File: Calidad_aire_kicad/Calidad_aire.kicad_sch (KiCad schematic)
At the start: 10 parts, among them J1 Micro_SD_Card, U1 DOIT-ESP32-DEVKIT-V1

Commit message: start to PCB design
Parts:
- A1, A4: footprint (none) -> footprint_project:header_4pos_1row
- U1: footprint (none) -> footprint_project:ESP32_DEVKIT1
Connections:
- net 3.3V: now also A4.3 (VCC), U1.16 (3V3); no longer A4. (VCC), U1.19 (3V3)
- net 5V: now also A1.1 (5V), A2.3 (5V), A3.3 (5V), U1.15 (VIN); no longer A1. (GND), A2. (TX), A3. (TX), U1.18 (VIN)
- net GND: now also A1.2 (GND), A2.4 (GND), A3.4 (GND), A4.4 (GND), A5.3 (NC), U1.14 (GND); no longer A1. (GND), A2. (TX), A3. (TX), A4. (VCC), A5.4 (GND), U1.17 (GND)
- net RX0_3V: now also A2.2 (TX); no longer A2. (TX)
- net RX0_5V: now also U1.27 (GPIO3__UART0-RX); no longer U1.33 (GPIO3__UART0-RX)
- net RX2_3V: now also A3.2 (TX); no longer A3. (TX)
- net RX2_5V: now also U1.21 (GPIO16_UART2-RX); no longer U1.27 (GPIO16_UART2-RX)
- net SCK: now also A4.2 (SCK), U1.29 (GPIO22_I2C-SCL); no longer A4. (VCC), U1.35 (GPIO22_I2C-SCL)
- net SDA: now also A4.1 (SDA), U1.26 (GPIO21_I2C-SDA); no longer A4. (VCC), U1.32 (GPIO21_I2C-SDA)
- net SD_CLK: now also U1.24 (GPIO18_VSPI-CLK); no longer U1.30 (GPIO18_VSPI-CLK)
- net SD_MISO: now also U1.25 (GPIO19_VSPI-MISO); no longer U1.31 (GPIO19_VSPI-MISO)
- net SD_MOSI: now also U1.30 (GPIO23_VSPI-MOSI); no longer U1.36 (GPIO23_VSPI-MOSI)
- net SD_SS: now also U1.23 (GPIO5_VSPI-CS0); no longer U1.29 (GPIO5_VSPI-CS0)
- net TX0_3V: now also A2.1 (RX); no longer A2. (TX)
- net TX0_5V: now also U1.28 (GPIO1_UART0-TX); no longer U1.34 (GPIO1_UART0-TX)
- net TX2_3V: now also A3.1 (RX); no longer A3. (TX)
- net TX2_5V: now also U1.22 (GPIO17_UART2-TX); no longer U1.28 (GPIO17_UART2-TX)
- net at R1.1: now also A1.3 (DO); no longer A1. (GND)
- no-connect marks 6 -> 24
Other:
- moved on the sheet: J1

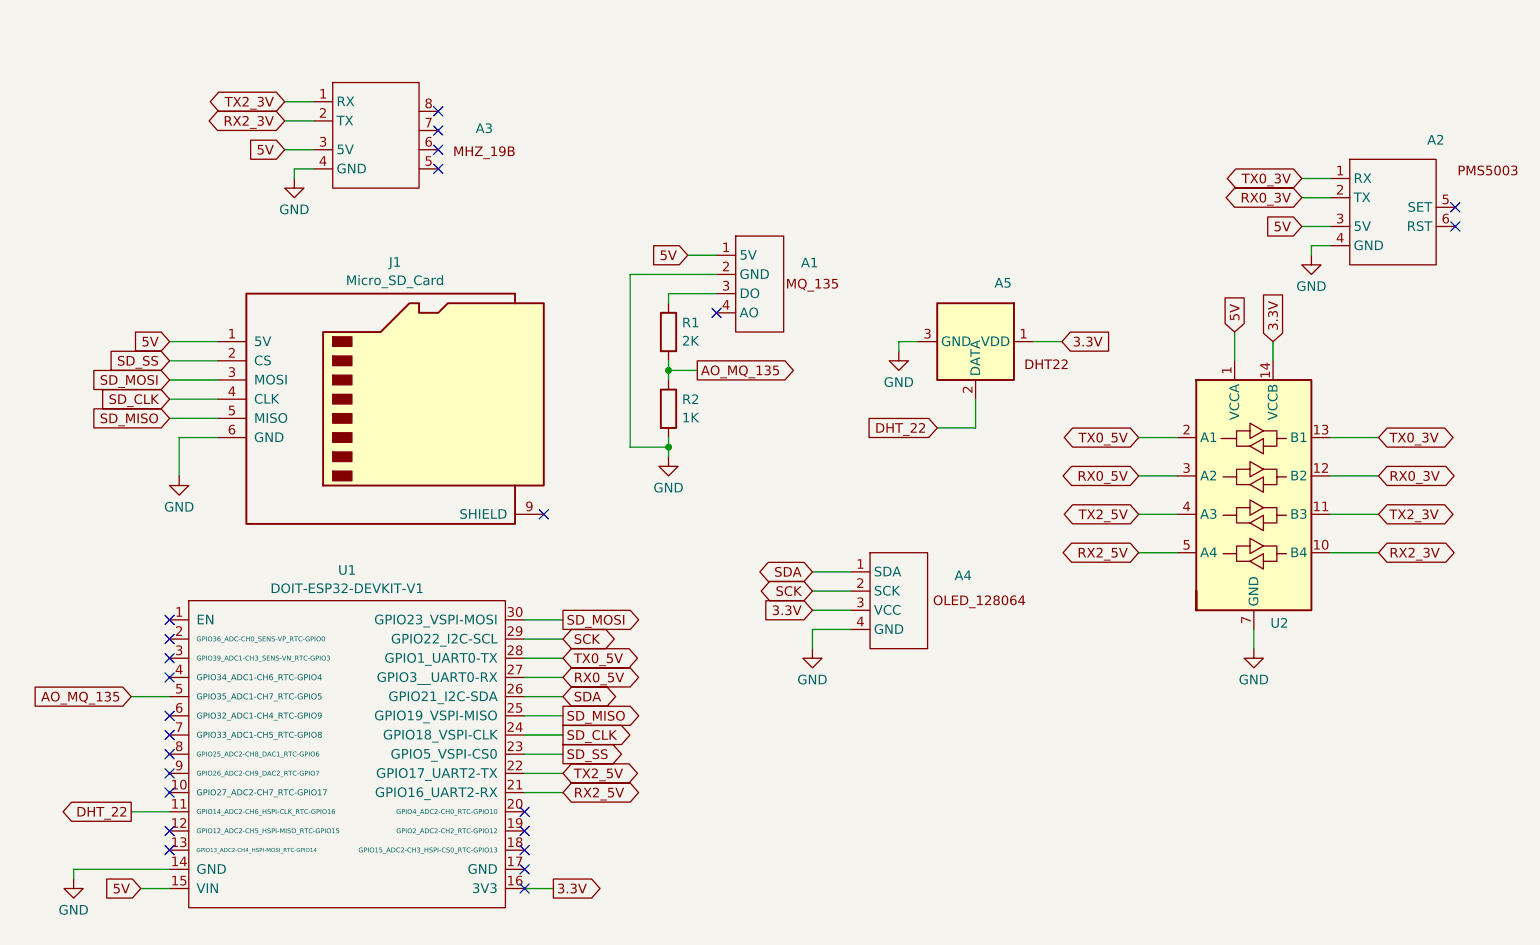
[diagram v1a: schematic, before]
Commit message: design of the footprints for the components
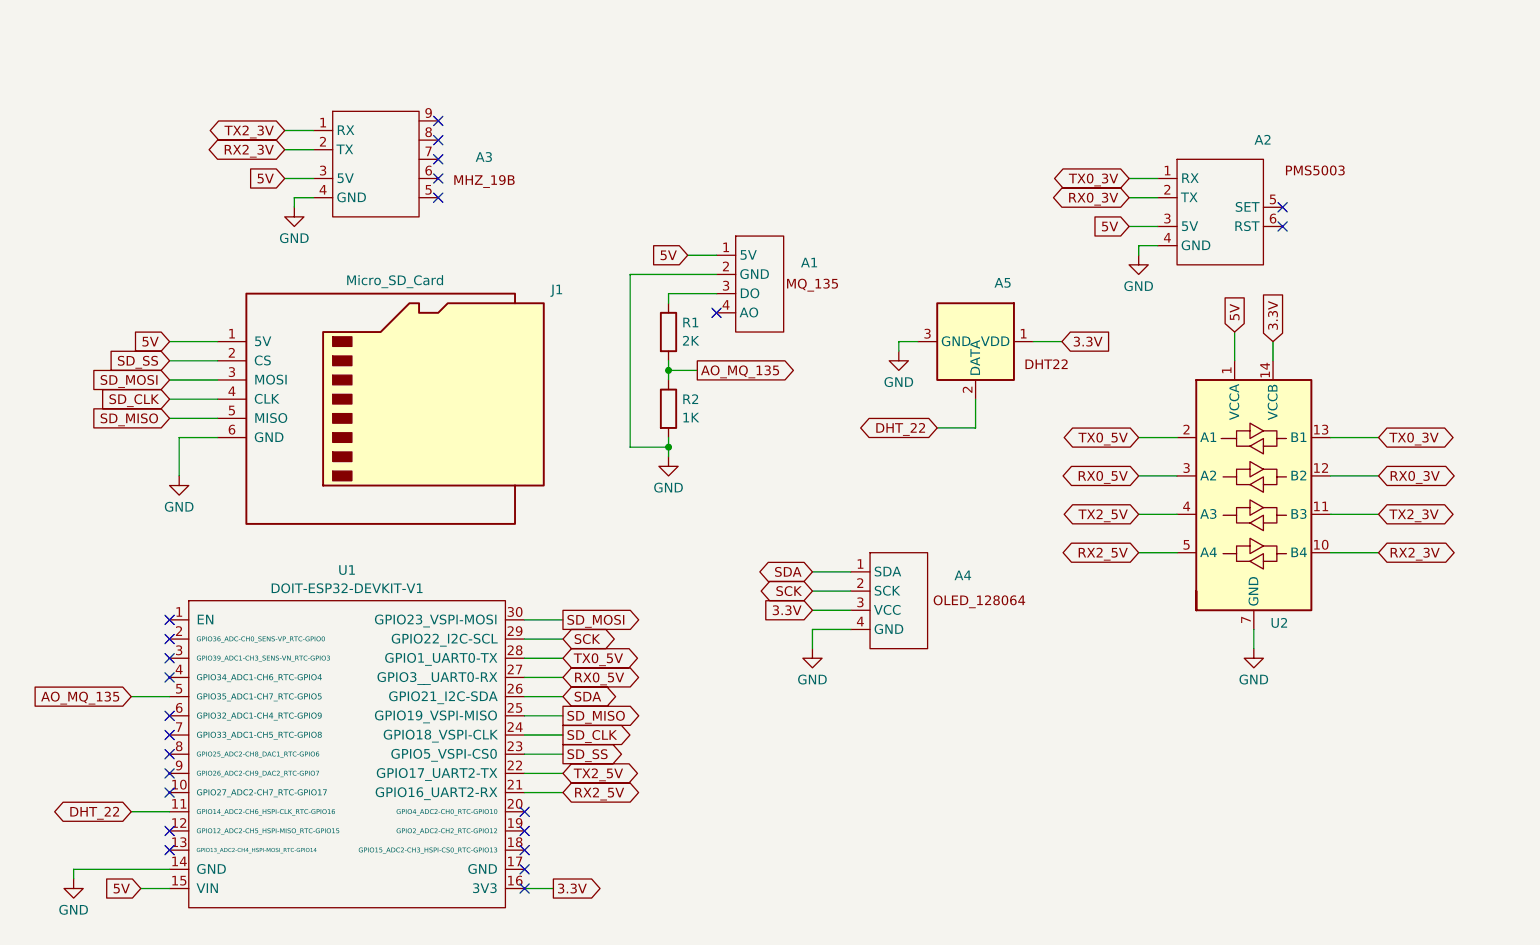
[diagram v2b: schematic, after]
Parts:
- A1: footprint footprint_project:header_4pos_1row -> footprint_project:MQ_135
- A2: footprint (none) -> TerminalBlock:TerminalBlock_bornier-4_P5.08mm
- A3: footprint (none) -> footprint_project:MH_Z19B
- A4: footprint footprint_project:header_4pos_1row -> footprint_project:OLED_128064
- A5: footprint (none) -> footprint_project:DHT22
- J1: footprint (none) -> footprint_project:microSD
- U2: footprint (none) -> footprint_project:conv_niv_log
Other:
- moved on the sheet: A2

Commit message: PCB design actualization
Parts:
- added BT1: Battery_Cell, TerminalBlock:TerminalBlock_bornier-2_P5.08mm, symbol Device:Battery_Cell
- added U3: ~, footprint_project:USB_TP4056, symbol symbols:USB_TPC4056
- R1, R2: footprint (none) -> Resistor_THT:R_Axial_DIN0414_L11.9mm_D4.5mm_P15.24mm_Horizontal
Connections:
- net 3.3V: now also U1.20 (GPIO4_ADC2-CH0_RTC-GPIO10)
- net 5V: now also U3.1 (VOUT+)
- net GND: now also BT1.2 (-), U3.2 (VOUT-), U3.6 (BAT-)
- net RX0_3V: now also U1.12 (GPIO12_ADC2-CH5_HSPI-MISO_RTC-GPIO15); no longer A2.2 (TX)
- net RX0_5V: now also A2.2 (TX); no longer U1.27 (GPIO3__UART0-RX)
- net RX2_3V: now also U1.21 (GPIO16_UART2-RX); no longer A3.2 (TX)
- net RX2_5V: now also A3.2 (TX); no longer U1.21 (GPIO16_UART2-RX)
- net TX0_3V: now also U1.13 (GPIO13_ADC2-CH4_HSPI-MOSI_RTC-GPIO14); no longer A2.1 (RX)
- net TX0_5V: now also A2.1 (RX); no longer U1.28 (GPIO1_UART0-TX)
- net TX2_3V: now also U1.22 (GPIO17_UART2-TX); no longer A3.1 (RX)
- net TX2_5V: now also A3.1 (RX); no longer U1.22 (GPIO17_UART2-TX)
- new net: BT1.1 (+), U3.5 (BAT+)
- no-connect marks 24 -> 21
